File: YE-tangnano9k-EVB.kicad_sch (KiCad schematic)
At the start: 27 parts, among them J1 Conn_01x24_Socket, J2 Conn_01x24_Socket, Q1 2SC1815, SW1 SW_SPDT, SW2 SW_Push, SW3 SW_Push, SW4 SW_Push, SW5 SW_Push, SW6 SW_Push, U1 Tang Nano 9K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

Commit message: fix net_name
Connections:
- net BUZZ renamed bz
- net DIG1 renamed com_1
- net DIG2 renamed com_2
- net DIG3 renamed com_3
- net DIG4 renamed com_4
- net LED_A renamed seg_a
- net LED_B renamed seg_b
- net LED_C renamed seg_c
- net LED_D renamed seg_d
- net LED_E renamed seg_e
- net LED_F renamed seg_f
- net LED_G renamed seg_g
- net Push1 renamed Push_1
- net Push2 renamed Push_2
- net Push3 renamed Push_3
- net Push4 renamed Push_4
- net Push5 renamed Push_5
- net SW_IN renamed SYS_EN
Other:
- note added: "buzzer"

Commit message: change pushSW net change buzzer logic(ActiveHigh → ActiveLow)
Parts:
- removed Q1: 2SC1815, Package_TO_SOT_THT:TO-92_Inline_Wide, symbol Transistor_BJT:2SC1815
- removed R12, R13, R14, R15: 680, Resistor_THT:R_Axial_DIN0207_L6.3mm_D2.5mm_P10.16mm_Horizontal, symbol Device:R_Small_US
- removed SW4, SW5, SW6: SW_Push, Button_Switch_THT:SW_PUSH_6mm_H7.3mm, symbol Switch:SW_Push
- added Q1: 2SA1015, Package_TO_SOT_THT:TO-92_Inline_Wide, symbol Transistor_BJT:2SA1015
- R11: value 680 -> 10k
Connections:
- net Push_2 is gone; now on net IOR15A: J1.19 (Pin_19), U1.19 (PIN54_IOR15A_RGB_B3)
- net Push_4 is gone; now on net IOR14A: J1.21 (Pin_21), U1.21 (PIN56_IOR14A_RGB_G6)
- net +5V: now also R11.1, Q1.1 (E); no longer BZ1.1 (+)
- net GND: now also BZ1.2 (-); no longer SW2.1, SW3.1
- net bz: now also R8.2; no longer R8.1
- net IOR14A: now reaches SW3.2
- net IOR15A: now reaches SW2.2
- net IOR15A: no longer R11.1
- net Push_1 renamed IOR15B
- net IOR15B: now also SW2.1; no longer R11.2
- net Push_3 renamed IOR14B
- net IOR14B: now also SW3.1
- net Push_5: no longer names the net of J1.22 (Pin_22), U1.22 (PIN57_IOR13A_RGB_G5)
- new net: BZ1.1 (+), Q1.2 (C)
- new net: Q1.3 (B), R11.2, R8.1
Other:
- moved on the sheet: BZ1, R8, SW2, SW3

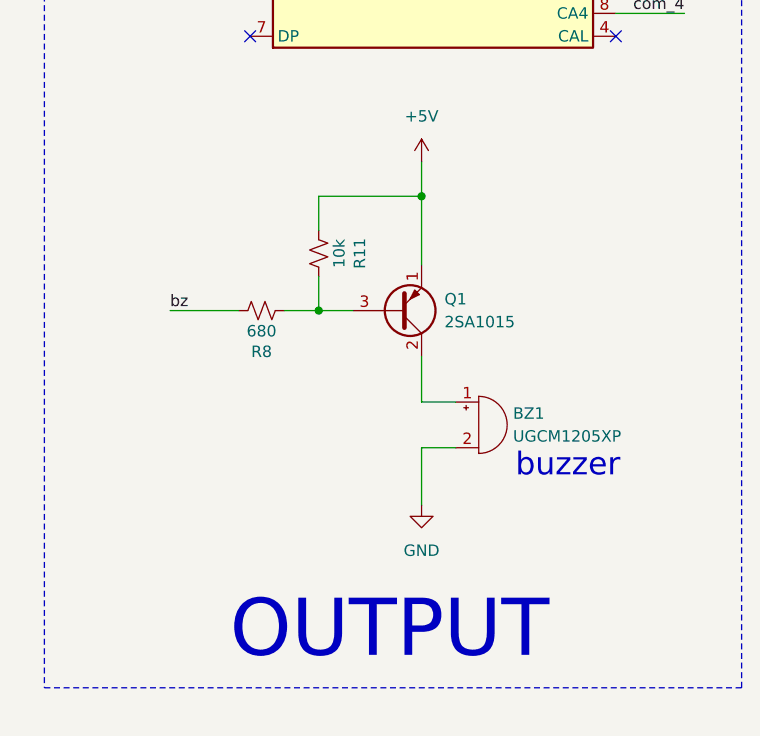
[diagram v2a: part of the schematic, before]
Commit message: change Buzzer_logic (→ActiveHIGH) fix pcb
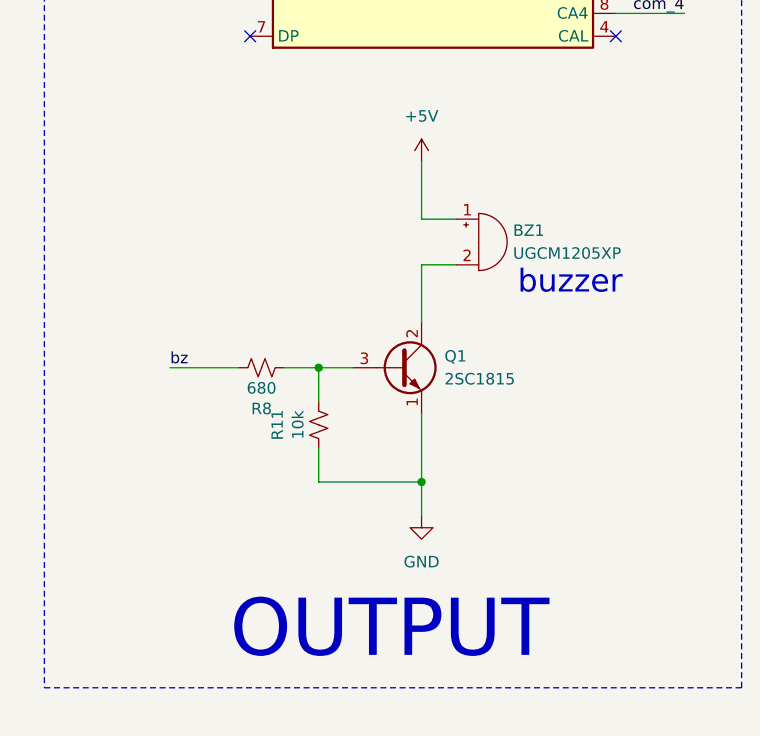
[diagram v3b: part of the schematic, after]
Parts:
- removed Q1: 2SA1015, Package_TO_SOT_THT:TO-92_Inline_Wide, symbol Transistor_BJT:2SA1015
- added Q1: 2SC1815, Package_TO_SOT_THT:TO-92_Inline_Wide, symbol Transistor_BJT:2SC1815
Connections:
- net +5V: now also BZ1.1 (+); no longer R11.1
- net GND: now also R11.1, Q1.1 (E); no longer BZ1.2 (-)
- net at R11.2, R8.1: now also Q1.3 (B)
- new net: BZ1.2 (-), Q1.2 (C)
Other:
- moved on the sheet: BZ1, R11, R8
